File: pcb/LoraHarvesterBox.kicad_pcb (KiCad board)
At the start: 4 copper layers, 48 x 45.5 mm, 44 parts, among them J1 Conn_01x02_Pin, J2 Conn_01x02_Pin, J3 Conn_01x02_Pin, J4 Conn_01x04_Socket, J5 Conn_01x04_Socket, J6 Conn_01x04_Socket, J7 Conn_01x04_Socket, J8 Conn_01x06_Socket, J9 Conn_01x08_Socket, SW1 SSSS811101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

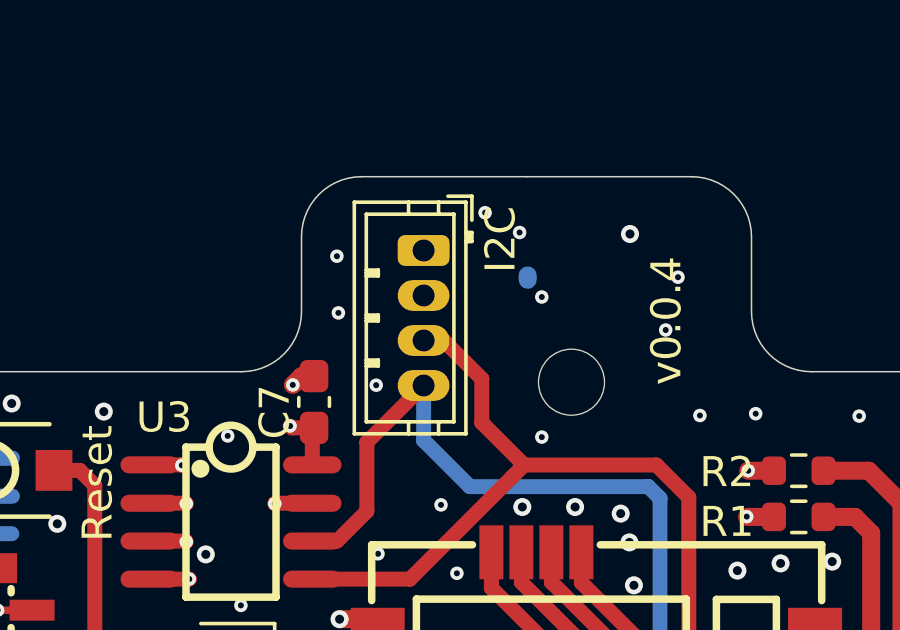
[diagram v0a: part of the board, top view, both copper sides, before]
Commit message: sch, pcb: clean up BOM
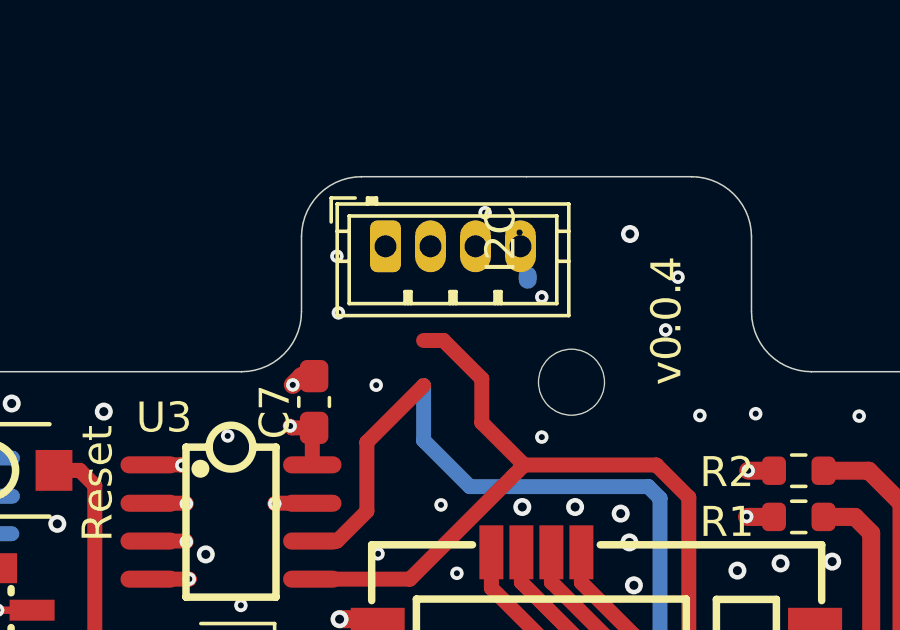
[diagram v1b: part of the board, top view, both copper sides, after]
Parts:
- C3: value 0.01uF -> 10nF
- C7, C8: value C -> 100nF
- C9: value 100nf -> 100nF
- moved J7 1.28 mm to (118.3, 56.8), turned to 0 degrees

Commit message: pcb: uploaded broken file by accident
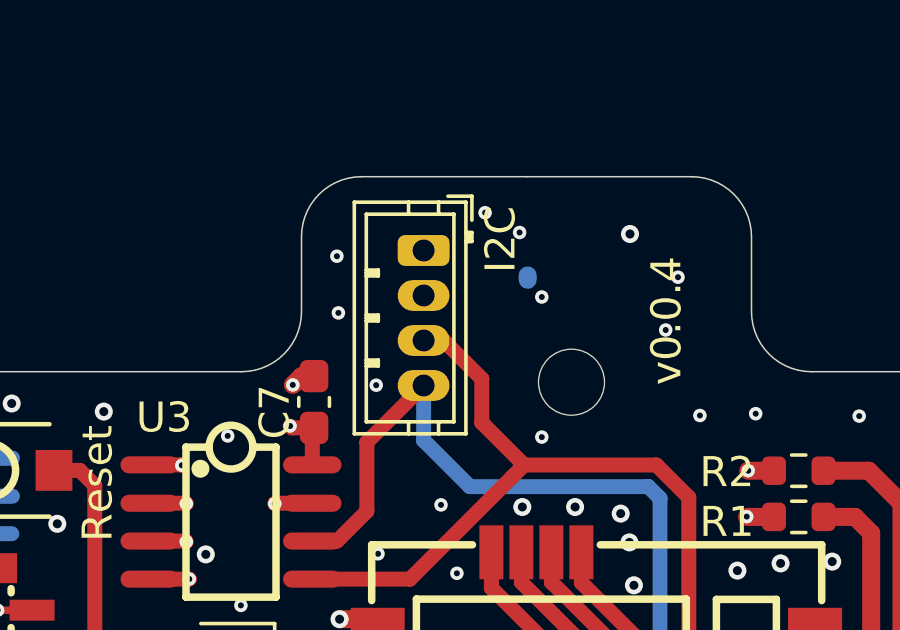
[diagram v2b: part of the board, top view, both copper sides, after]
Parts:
- moved J7 1.28 mm to (119.6, 57.0), turned to -90 degrees

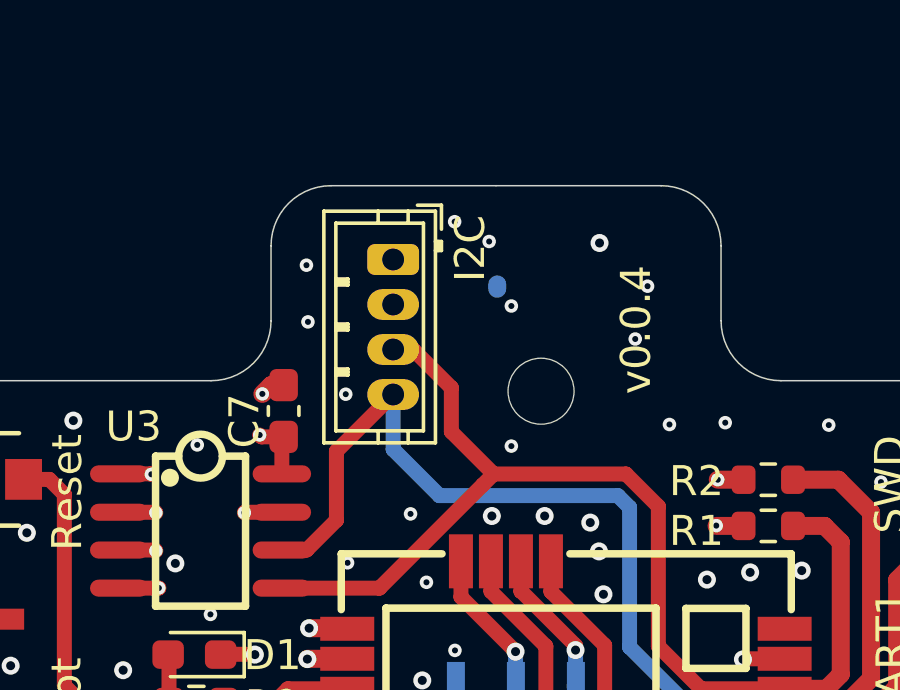
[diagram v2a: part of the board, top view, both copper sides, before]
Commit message: pcb, doc: improve silk prints of I2C connector
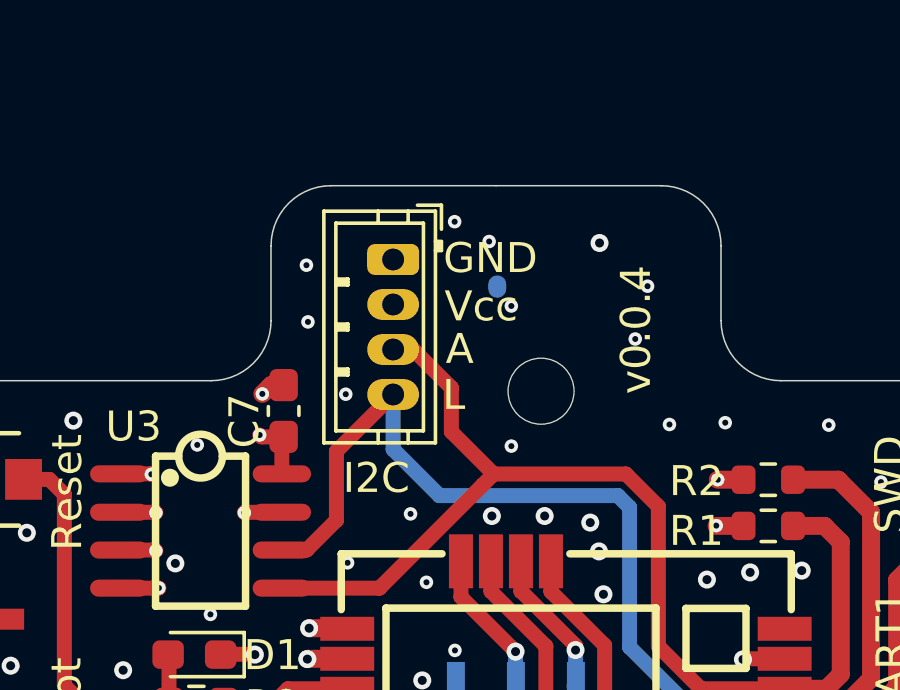
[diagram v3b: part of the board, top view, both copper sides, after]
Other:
- board text added: "A"
- board text added: "L"
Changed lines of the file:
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@@
+		)
+	)
+	(gr_text "I2C"
+		(at 117.89 64.83 0)
+		(layer "F.SilkS")
+		(effects
+			(font
+				(size 1 1)
+				(thickness 0.125)
+			)
+			(justify left bottom)
 		)
 	)
@@
 		)
 	)
-	(gr_text "I2C"
-		(at 122.72 57.71 90)
+	(gr_text "GND"
+		(at 121.24 57.5 0)
 		(layer "F.SilkS")
 		(effects
@@
 		)
 	)
+	(gr_text "L"
+		(at 121.21 62.06 0)
+		(layer "F.SilkS")
+		(effects
+			(font
+				(size 1 1)
+				(thickness 0.125)
+			)
+			(justify left bottom)
+		)
+	)
+	(gr_text "Vcc"
+		(at 121.28 59.11 0)
+		(layer "F.SilkS")
+		(effects
+			(font
+				(size 1 1)
+				(thickness 0.125)
+			)
+			(justify left bottom)
+		)
+	)
 	(gr_text "+"
 		(at 115.19 81.47 90)
@@
 			)
 			(justify left bottom)
+		)
+	)
+	(gr_text "A"
+		(at 121.32 60.53 0)
+		(layer "F.SilkS")
+		(effects
+			(font
+				(size 1 1)
+				(thickness 0.125)
+			)
+			(justify left bottom)

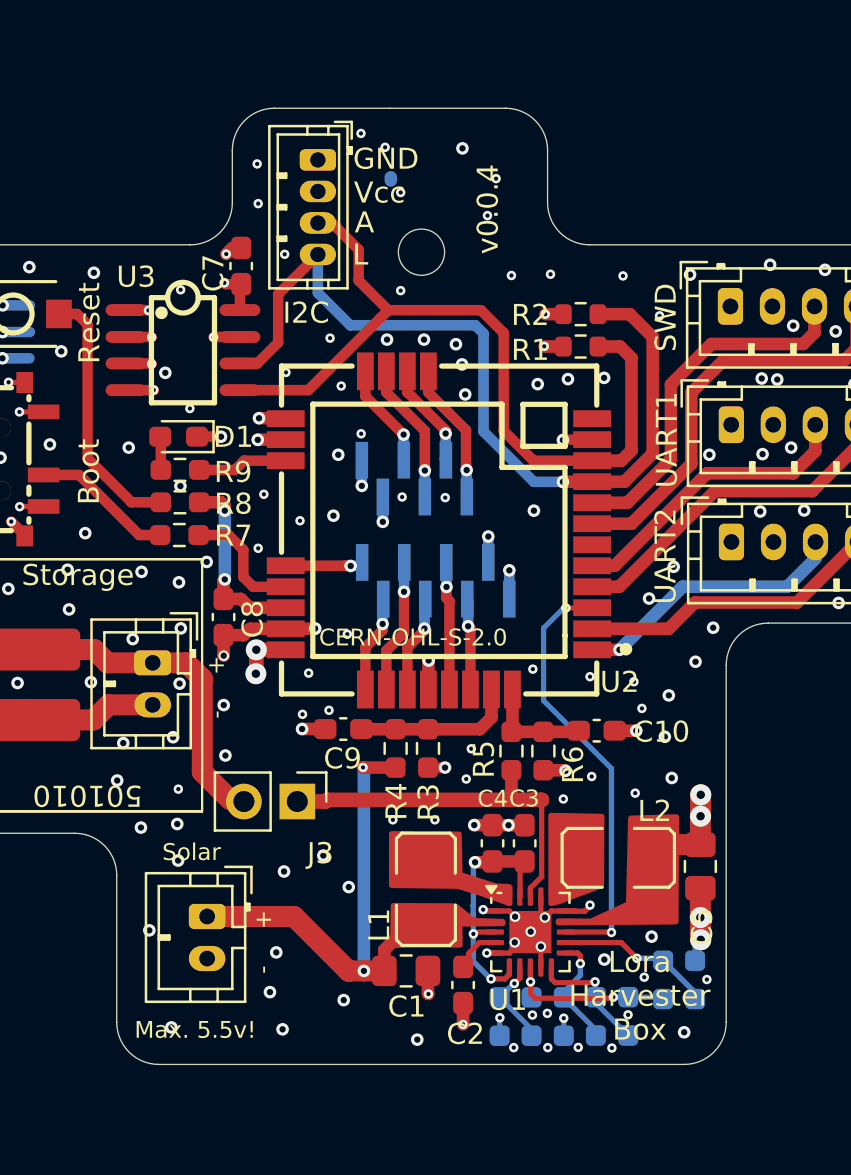
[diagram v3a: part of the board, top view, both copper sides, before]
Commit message: pcb, doc, sch: add load switch. VBAT_OK (optionally) can switch on/off the RAK3172
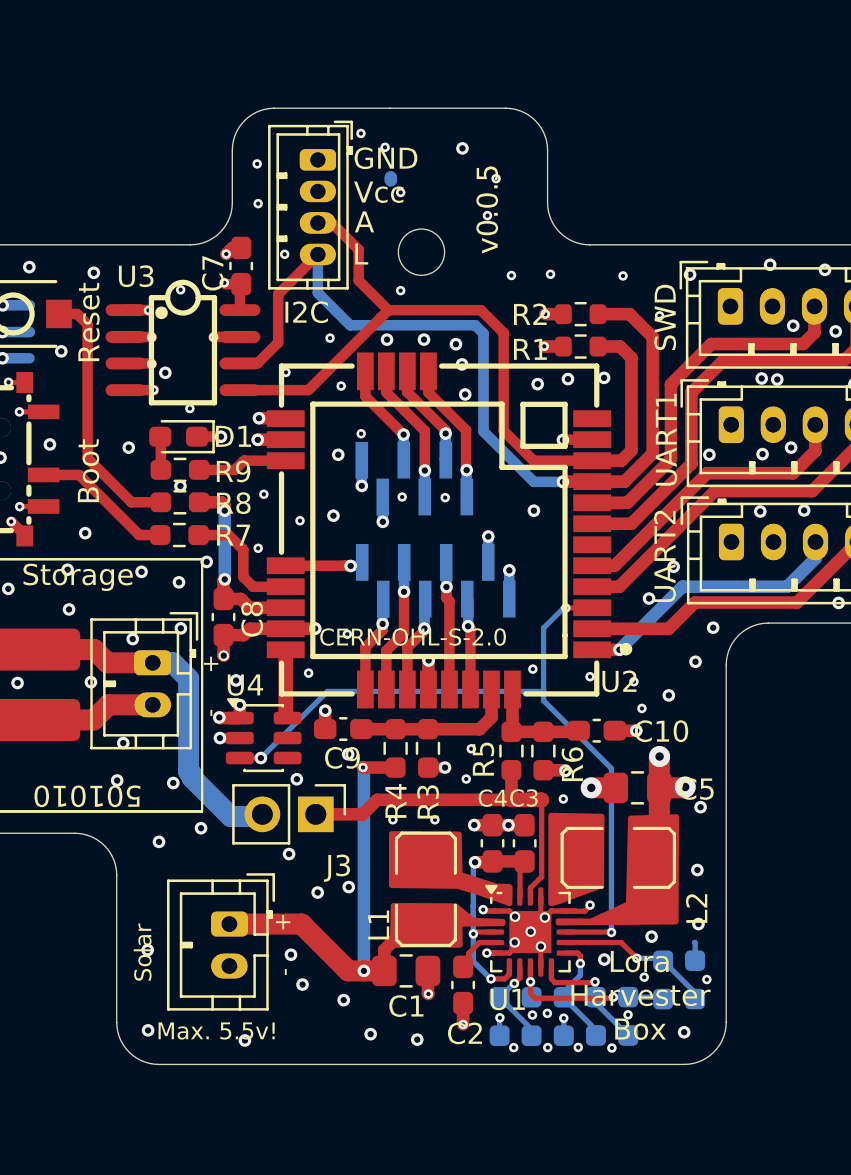
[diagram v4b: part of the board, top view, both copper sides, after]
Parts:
- added U4: TPS22917DBV, Package_TO_SOT_SMD:SOT-23-6, F.Cu at (117.0, 84.5)
- moved C5 4.79 mm to (134.8, 86.8), turned to 0 degrees
- moved J1 1.12 mm to (115.4, 93.3)
- moved J3 1.07 mm to (119.5, 88.1)
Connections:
- U2 pad 24: +3V0 -> /Vdd_Input
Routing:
- net /VBAT_OK: track 20.7 -> 36.5 mm, vias 2 -> 3
- net /Vdd_Input: track 0.00 -> 3.29 mm
- net +3V0: track 13.3 -> 15.1 mm
- net Net-(BT1-+): track 16.3 -> 17.7 mm
- net /VSOLAR: track 25.7 -> 24.5 mm
- net /VBAT: track 17.9 -> 17.3 mm
- net GND: track 60.4 -> 59.8 mm, vias 180 -> 176
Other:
- board text added: "v0.0.5"
- board text removed: "v0.0.4"
